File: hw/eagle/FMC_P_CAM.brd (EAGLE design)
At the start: 100 x 80 mm, 1 part, among them J1 FMC-LPC

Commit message: update board
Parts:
- added U1: SN74AVCH16T245_DGV_48, SN74AVCH16T245_DGV_48:DGV48
- moved J1 6.48 mm to (17.8, 34.3)
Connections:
- removed net VADJ: J1.H40
- new net +12V: J1.C35, J1.C37
- new net +3V3: J1.C39, J1.D36, J1.D38, J1.D40
- new net FMC_CAM1_D0: J1.D15
- new net FMC_CAM1_D1: J1.D14
- new net FMC_CAM1_D2: J1.C15
- new net FMC_CAM1_D3: J1.C14
- new net FMC_CAM1_D8: J1.D12
- new net FMC_CAM1_D9: J1.D11
- new net FMC_CAM1_HREF: J1.C11
- new net FMC_CAM1_PWDN: J1.C23
- new net FMC_CAM1_RST: J1.D8
- new net FMC_CAM1_VSYNC: J1.C10
- new net FMC_CAM2_HREF: J1.D21
- new net FMC_CAM2_PWDN: J1.C18
- new net FMC_CAM2_RSVD4: J1.D18
- new net FMC_CAM2_RSVD5: J1.D17
- new net FMC_CAM2_RSVD6: J1.C19
- new net FMC_CAM2_VSYNC: J1.D20
- new net FMC_DVO_D10: J1.D24
- new net FMC_DVO_D11: J1.D23
- new net FMC_DVO_D6: J1.D27
- new net FMC_DVO_D7: J1.D26
- new net FMC_DVO_D8: J1.C27
- new net FMC_DVO_D9: J1.C26
- new net FMC_DVO_IDCK+: J1.C22
- new net FMC_GA0: J1.C34
- new net FMC_GA1: J1.D35
- new net FMC_GPIO3: J1.D9
- new net FMC_SCL: J1.C30
- new net FMC_SDA: J1.C31
- new net N$4: J1.D30, J1.D31
- new net PG_C2M: J1.D1
- net FMC_CAM1_RSVD0: now also U1.22
- net FMC_CAM1_RSVD1: now also U1.20
- net FMC_CAM1_RSVD2: now also U1.19
- net FMC_CAM1_RSVD3: now also U1.17
- net FMC_CAM1_RSVD4: now also U1.16
- net FMC_CAM1_RSVD6: now also U1.13
- net GND: now also J1.C1, J1.C12, J1.C13, J1.C16, J1.C17, J1.C20, J1.C21, J1.C24, J1.C25, J1.C28, J1.C29, J1.C32, J1.C33, J1.C36, J1.C38, J1.C4, J1.C40, J1.C5, J1.C8, J1.C9, J1.D10, J1.D13, J1.D16, J1.D19, J1.D2, J1.D22, J1.D25, J1.D28, J1.D3, J1.D37, J1.D39, J1.D6, J1.D7, U1.10, U1.15, U1.21, U1.28, U1.34, U1.39, U1.4, U1.45
- net VDD: now also J1.H40, U1.18, U1.31, U1.42, U1.7

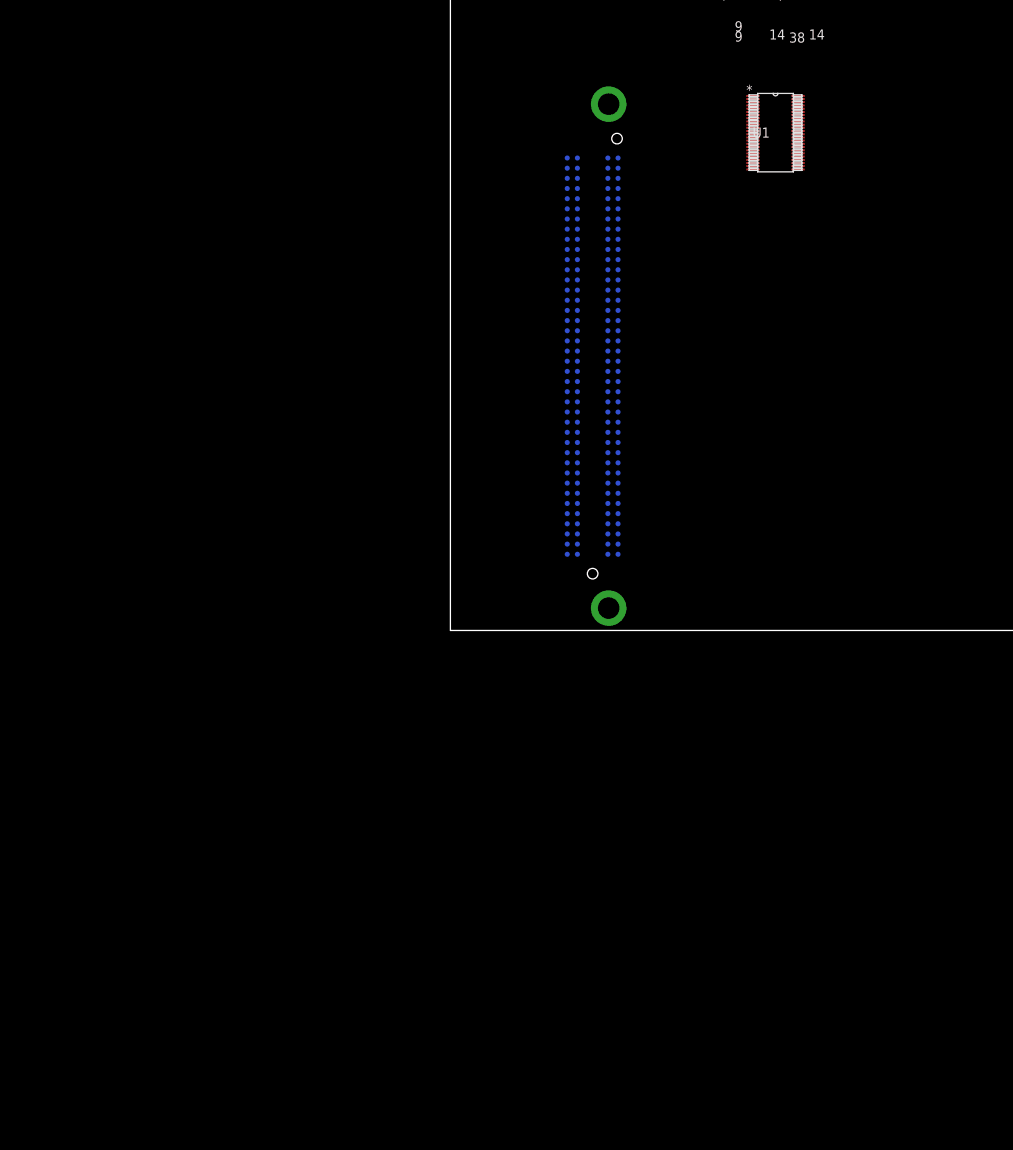
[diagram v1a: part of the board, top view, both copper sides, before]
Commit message: update schematic
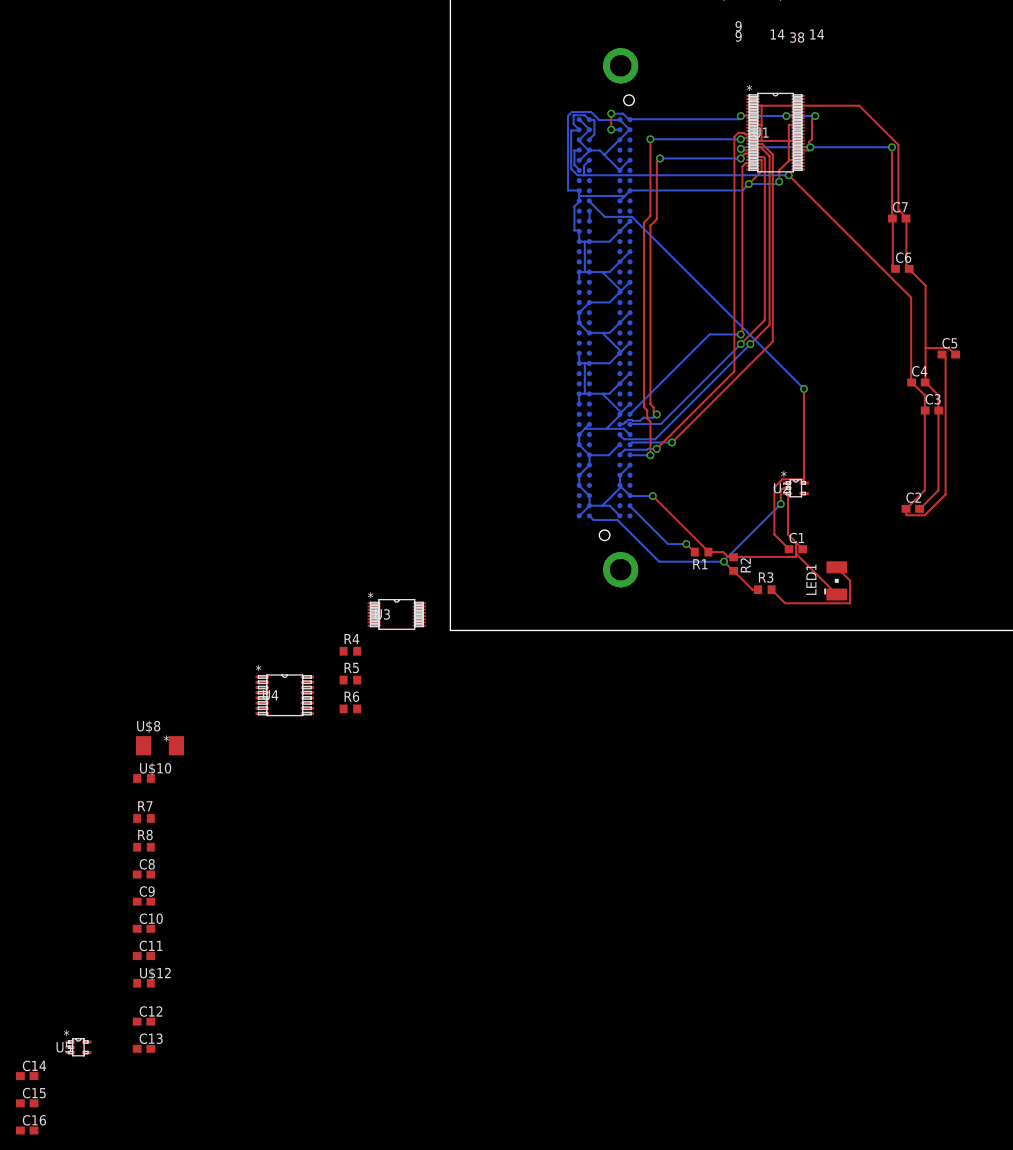
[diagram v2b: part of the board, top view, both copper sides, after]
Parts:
- added C1, C2, C3, C4, C5, C6, C7: (no value), resistor:C0603
- added C10, C11, C12, C13, C14, C15, C16, C8, C9: (no value), my-rcl:C0603
- added LED1: LY_T679-D2E2-1, led:PLCC2
- added R1, R2, R3: 4K7, resistor:R0603
- added R4, R5, R6, R7, R8: (no value), resistor:R0603
- added U$10, U$12: L-MY, my-rcl:R0603
- added U$8: (no value), CX5032GB (CX-53F):CX5032GB
- added U2: SN74LVC1G14_DCK_5, SN74LVC1G14_DCK_5:DCK5
- added U3: PCA9546A_DGV_16, PCA9546A_DGV_16:DGV16
- added U4: CDCE925_PW_16, CDCE925_PW_16:PW16
- added U5: TPS71718_DCK_5, TPS71718_DCK_5:DCK5
- moved J1 5.03 mm to (19.3, 39.1)
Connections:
- net +12V renamed 12P0V
- removed net +3V3: J1.C39, J1.D36, J1.D38, J1.D40
- removed net VDD: J1.G39, J1.H40, U1.18, U1.31, U1.42, U1.7
- new net 3P3AUX: C1.1, J1.D32, U2.5
- new net 3P3V: C14.1, C2.1, C3.1, C4.1, C5.1, J1.C39, J1.D36, J1.D38, J1.D40, U1.24, U1.31, U1.42, U5.1, U5.3
- new net CAM1_SCL: U3.7
- new net CAM1_SDA: U3.6
- new net CAM2_SCL: U3.5
- new net CAM2_SDA: U3.4
- new net EN#: U1.25, U1.48, U2.4
- new net HDMI_SCL: U3.12
- new net HDMI_SDA: U3.11
- new net N$10: C12.1, U4.7
- new net N$11: C13.1, U4.8
- new net N$13: C15.1, U5.4
- new net N$2: LED1.A, R3.2
- new net N$3: U$8.2, U4.1
- new net N$5: U$8.1, U4.16
- new net N$6: C8.1, R7.2, R8.2, U$10.2, U4.3
- new net N$7: R8.1, U4.2
- new net N$8: R7.1, U4.4
- new net N$9: C10.1, C11.1, U$12.2, U4.6, U4.9
- new net REG_1P8V: C16.1, U$10.1, U5.5
- new net TMDS_PLL_SCL: U3.10, U4.14
- new net TMDS_PLL_SDA: U3.9, U4.15
- new net VADJ: C6.1, C7.1, C9.1, J1.G39, J1.H40, R4.2, R5.2, R6.2, U$12.1, U1.18, U1.7, U3.16
- net FMC_CAM1_PCLK: now also U1.23
- net FMC_CAM1_PWDN: now also U1.3
- net FMC_CAM1_RST: now also U1.2
- net FMC_CAM1_RSVD5: now also U1.14
- net FMC_CAM2_PWDN: now also U1.12
- net FMC_CAM2_RST: now also U1.11
- net FMC_FRSTN_M2C_L: now also R1.2
- net GND: now also C1.2, C10.2, C11.2, C14.2, C15.2, C16.2, C2.2, C3.2, C4.2, C5.2, C6.2, C7.2, C8.2, LED1.C, R1.1, R2.1, U1.1, U2.3, U3.1, U3.13, U3.2, U3.8, U4.12, U4.5, U5.2
- net I2C_SW_RST: now also R4.1, U3.3
- net MUX_SCL: now also R6.1, U3.14
- net MUX_SDA: now also R5.1, U3.15
- net PG_C2M: now also R2.2, R3.1, U2.2
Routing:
- net GND: track 0.00 -> 322.1 mm, vias 0 -> 3
- net 3P3V: track 0.00 -> 117.5 mm, vias 0 -> 1
- net VADJ: track 0.00 -> 74.5 mm, vias 0 -> 8
- net 3P3AUX: track 0.00 -> 61.0 mm, vias 0 -> 1
- net FMC_CAM1_RSVD5: track 0.00 -> 55.7 mm, vias 0 -> 3
- net FMC_CAM1_RSVD6: track 0.00 -> 50.6 mm, vias 0 -> 1
- net FMC_CAM1_RSVD2: track 0.00 -> 50.0 mm, vias 0 -> 3
- net FMC_CAM1_RSVD4: track 0.00 -> 49.6 mm, vias 0 -> 1
- net FMC_CAM1_RSVD3: track 0.00 -> 48.6 mm, vias 0 -> 1
- net FMC_CAM1_RSVD1: track 0.00 -> 44.0 mm, vias 0 -> 1
- net FMC_CAM1_RSVD0: track 0.00 -> 40.6 mm, vias 0 -> 1
- net PG_C2M: track 0.00 -> 37.8 mm, vias 0 -> 2
- net N$2: track 0.00 -> 15.7 mm
- net FMC_FRSTN_M2C_L: track 0.00 -> 10.5 mm, vias 0 -> 1
- net 12P0V: track 0.00 -> 3.39 mm
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
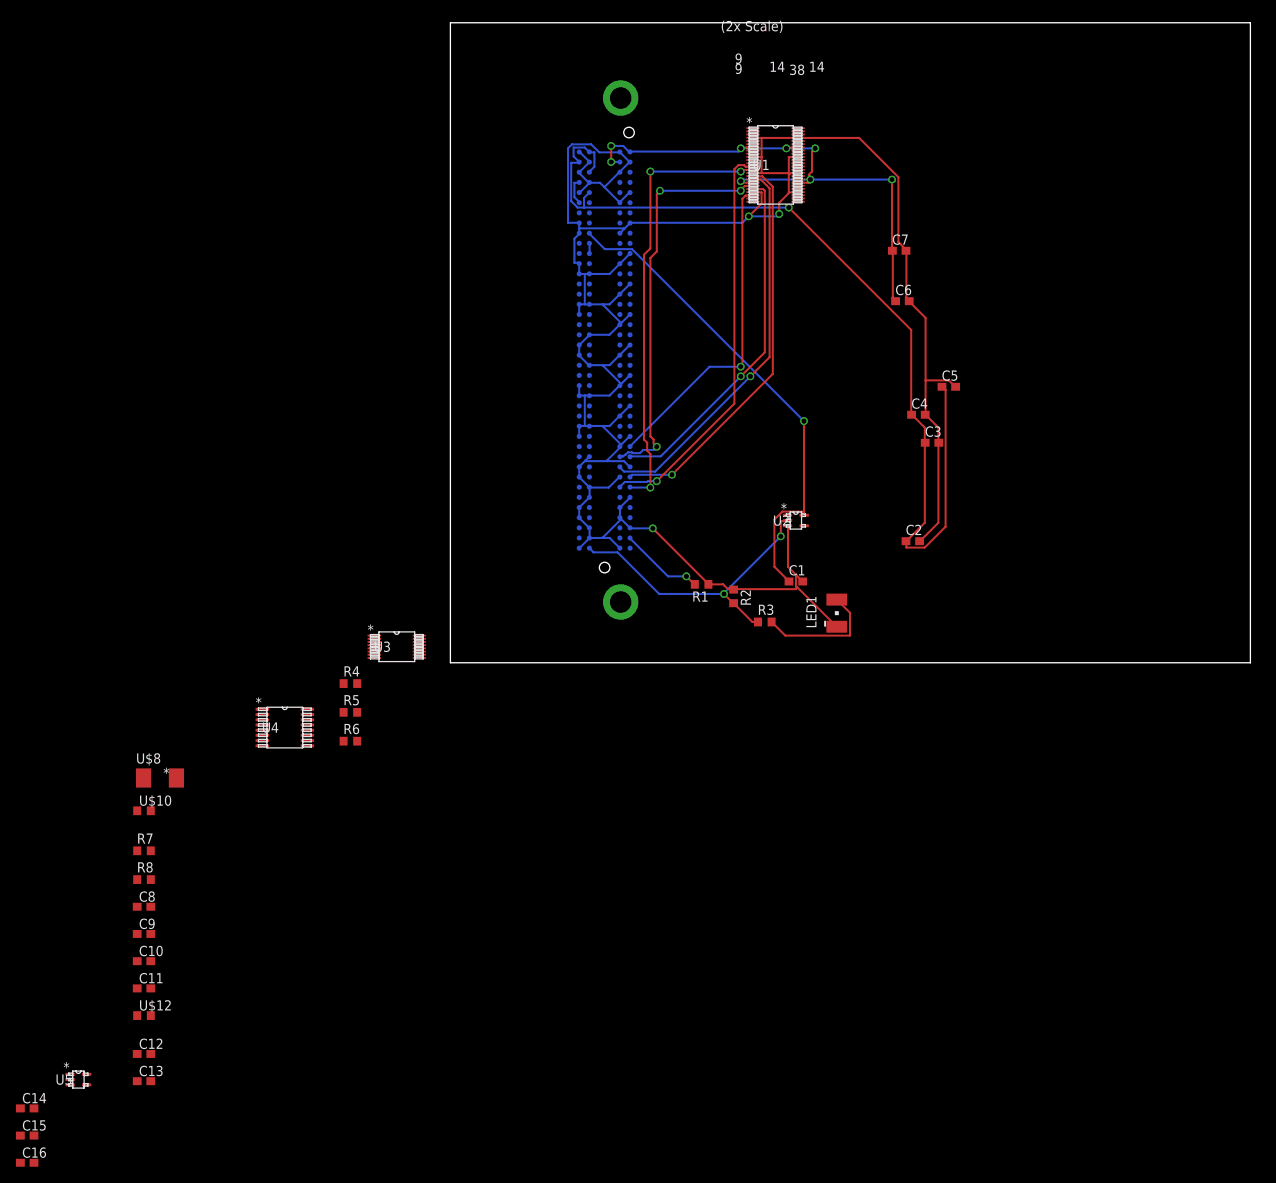
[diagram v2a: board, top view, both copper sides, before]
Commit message: add user defined library
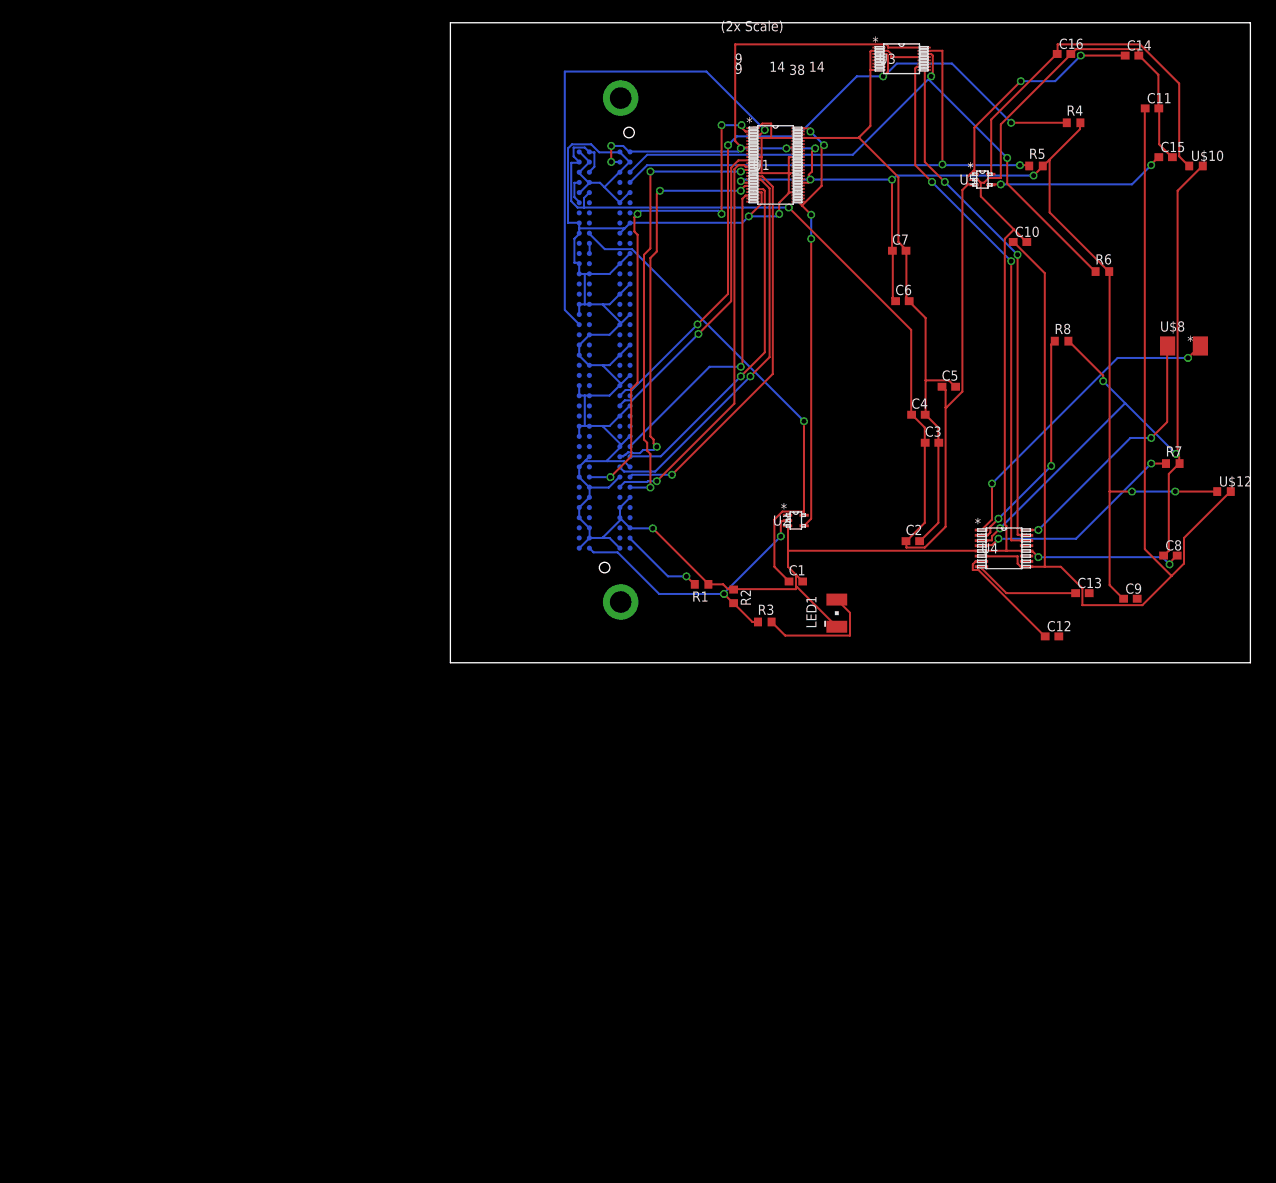
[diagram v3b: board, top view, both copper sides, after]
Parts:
- moved C14 190.8 mm to (85.2, 75.9)
- moved C16 189.8 mm to (76.7, 76.1)
- moved C15 187.6 mm to (89.4, 63.2)
- moved C11 167.3 mm to (87.7, 69.3)
- moved U5 159.5 mm to (66.5, 60.4)
- moved U$10 154.2 mm to (93.2, 62.1)
- moved U$12 150.1 mm to (96.7, 21.4)
- moved C10 141.7 mm to (71.2, 52.6)
- moved U$8 138.9 mm to (91.7, 39.6)
- moved R7 137.4 mm to (90.3, 24.9)
- moved C8 135.6 mm to (90.0, 13.4)
- moved R8 133.0 mm to (76.4, 40.2)
- moved C13 132.2 mm to (79.0, 8.70)
- moved C9 130.2 mm to (85.0, 8.00)
- moved C12 124.9 mm to (75.2, 3.30)
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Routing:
- net GND: track 322.1 -> 494.0 mm, vias 3 -> 5
- net N$9: track 0.00 -> 145.4 mm
- net VADJ: track 74.5 -> 210.9 mm, vias 8 -> 11
- net N$6: track 0.00 -> 96.5 mm, vias 0 -> 3
- net I2C_SW_RST: track 0.00 -> 91.1 mm, vias 0 -> 4
- net MUX_SCL: track 0.00 -> 79.6 mm, vias 0 -> 2
- net MUX_SDA: track 0.00 -> 67.5 mm, vias 0 -> 2
- net TMDS_PLL_SCL: track 0.00 -> 67.1 mm, vias 0 -> 2
- net TMDS_PLL_SDA: track 0.00 -> 64.2 mm, vias 0 -> 2
- net FMC_CAM1_RST: track 0.00 -> 63.6 mm, vias 0 -> 5
- net FMC_CAM1_PWDN: track 0.00 -> 62.1 mm, vias 0 -> 1
- net 3P3V: track 117.5 -> 178.1 mm, vias 1 -> 3
- net EN#: track 0.00 -> 54.6 mm, vias 0 -> 4
- net REG_1P8V: track 0.00 -> 47.8 mm
- net N$3: track 0.00 -> 39.5 mm, vias 0 -> 2
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
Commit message: update board schematic
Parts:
- removed C1: (no value), resistor:C0603
- removed R2: 4K7, resistor:R0603
- removed U$8: (no value), CX5032GB (CX-53F):CX5032GB
- added C101: 100nF, resistor:C0603
- added C305, C306, C307, C308, C309, C310, C311, C312, C313, C314, C315, C316, C503: 100nF, rcl:C0603
- added C500: 15nF, rcl:C0603
- added C501: 330pF, rcl:C0603
- added C502: 12pF, rcl:C0603
- added C507: 10uF 16V, rcl:C0603
- added C508: 47uF 10V, rcl:C0603
- added C509, C510: 2n2F, rcl:C0603
- added D1: MBRS130LT3, diode:SMB
- added PAD1, PAD10, PAD11, PAD2, PAD3, PAD4, PAD5, PAD6, PAD7, PAD8, PAD9: (no value), wirepad:1,6/0,8
- added Q1: 27MHz, special:Q
- added R106: 4K7 DNI, resistor:R0603
- added R202, R203, R205, R206, R207, R208, R209, R210: 4K7, resistor:R0603
- added R500: 348K, rcl:R0603
- added R501: 78K7, rcl:R0603
- added R502: 40K2, rcl:R0603
- added R503: 10K, rcl:R0603
- added R504: 1K87, rcl:R0603
- added R506: 36K5, rcl:R0603
- added U$23, U$24: L-MY, my-rcl:R0603
- added U6, U7: SN74AVCH16T245_DGV_48, SN74AVCH16T245_DGV_48:DGV48
- added U8: TPS54140_DGQ_10, TPS54140_DGQ_10:DGQ10_1P88X1P57
- C102, C103, C104, C105, C106, C107, C200, C201, C202, C203, C209, C210: value (none) -> 100nF
- C206, C208: value (none) -> 1uF
- C207: value (none) -> 10nF
- R105: value 4K7 -> 33R DNI
- R200, R201, R204, R212: value (none) -> 4K7
- R211: value (none) -> 4K7 DNI
- moved U2 47.3 mm to (34.1, 64.2), turned to 180 degrees
- moved U1 44.4 mm to (48.8, 18.6), flipped to the bottom, turned to 180.5 degrees
- moved U3 32.8 mm to (68.3, 44.9)
- moved U4 14.7 mm to (75.5, 27.6), turned to 90 degrees
- renumbered C10 to C202, C11 to C201, C12 to C209, C13 to C210, C14 to C206, C15 to C207, C16 to C208, C2 to C102, C3 to C103, C4 to C104, C5 to C105, C6 to C106, C7 to C107, C8 to C203, C9 to C200, R1 to R104, R3 to R105, R4 to R204, R5 to R201, R6 to R200, R7 to R211, R8 to R212
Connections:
- new net CAM1_XCLK: C210.2
- new net CAM2_XCLK: C209.2
- new net N$15: C507.1, C510.1, R500.2, U$23.2, U8.2
- new net N$16: C503.1, U8.1
- new net N$17: C503.2, D1.C, U$24.1, U8.10
- new net N$19: R500.1, R501.2, U8.3
- new net N$20: C500.1, U8.4
- new net N$21: R502.2, U8.5
- new net N$22: J1.H1, PAD1.1
- new net N$23: C502.1, R506.2, U8.8
- new net N$24: C501.1, R506.1
- new net N$25: R503.1, R504.2, U8.7
- new net N$26: J1.D4, PAD3.1
- new net N$27: J1.D5, PAD4.1
- new net N$28: J1.D29, PAD5.1
- new net N$29: J1.D33, PAD6.1
- new net N$30: J1.D34, PAD7.1
- new net N$31: J1.C2, PAD8.1
- new net N$32: J1.C3, PAD9.1
- new net N$33: J1.C6, PAD10.1
- new net N$34: J1.C7, PAD11.1
- new net PGOOD: U8.6
- new net REG_5P0V: C508.1, R209.2, R210.2, R503.2, U$24.2
- net 12P0V: now also C509.1, U$23.1
- net 3P3AUX: now also C101.1; no longer C1.1
- net 3P3V: now also C305.1, C306.1, C309.1, C310.1, C313.1, C314.1, R202.2, R203.2, R205.2, R206.2, R207.2, R208.2, U6.1, U6.24, U6.31, U6.42, U7.1, U7.24, U7.31, U7.42
- net CAM1_SCL: now also R203.1
- net CAM1_SDA: now also R202.1
- net CAM2_SCL: now also R206.1
- net CAM2_SDA: now also R205.1
- net EN#: now also U6.25, U6.48, U7.25, U7.48
- net FMC_CAM1_D0: now also U6.17
- net FMC_CAM1_D1: now also U6.16
- net FMC_CAM1_D2: now also U6.14
- net FMC_CAM1_D3: now also U6.13
- net FMC_CAM1_D4: now also U6.12
- net FMC_CAM1_D5: now also U6.11
- net FMC_CAM1_D6: now also U6.9
- net FMC_CAM1_D7: now also U6.8
- net FMC_CAM1_D8: now also U6.6
- net FMC_CAM1_D9: now also U6.5
- net FMC_CAM1_HREF: now also U6.3
- net FMC_CAM1_VSYNC: now also U6.2
- net FMC_CAM2_D0: now also U7.23
- net FMC_CAM2_D1: now also U7.22
- net FMC_CAM2_D2: now also U7.20
- net FMC_CAM2_D3: now also U7.19
- net FMC_CAM2_D4: now also U7.17
- net FMC_CAM2_D5: now also U7.16
- net FMC_CAM2_D6: now also U7.14
- net FMC_CAM2_D7: now also U7.13
- net FMC_CAM2_D8: now also U7.12
- net FMC_CAM2_D9: now also U7.11
- net FMC_CAM2_HREF: now also U7.9
- net FMC_CAM2_PCLK: now also U7.6
- net FMC_CAM2_RSVD0: now also U7.5
- net FMC_CAM2_RSVD1: now also U7.3
- net FMC_CAM2_RSVD2: now also U7.2
- net FMC_CAM2_RSVD3: now also U6.23
- net FMC_CAM2_RSVD4: now also U6.22
- net FMC_CAM2_RSVD5: now also U6.20
- net FMC_CAM2_RSVD6: now also U6.19
- net FMC_CAM2_VSYNC: now also U7.8
- net GND: now also C101.2, C200.2, C305.2, C306.2, C307.2, C308.2, C309.2, C310.2, C311.2, C312.2, C313.2, C314.2, C315.2, C316.2, C500.2, C501.2, C502.2, C507.2, C508.2, C509.2, C510.2, D1.A, R106.1, R501.1, R502.1, R504.1, U6.10, U6.15, U6.21, U6.28, U6.34, U6.39, U6.4, U6.45, U7.10, U7.15, U7.21, U7.28, U7.34, U7.39, U7.4, U7.45, U8.9; no longer C1.2, R2.1
- net HDMI_SCL: now also R210.1
- net HDMI_SDA: now also R209.1
- net N$1: now also PAD2.1
- net N$3: now also Q1.1; no longer U$8.2
- net N$5: now also Q1.2; no longer U$8.1
- net PG_C2M: now also R106.2; no longer R2.2
- net TMDS_PLL_SCL: now also R208.1
- net TMDS_PLL_SDA: now also R207.1
- net VADJ: now also C307.1, C308.1, C311.1, C312.1, C315.1, C316.1, U6.18, U6.7, U7.18, U7.7
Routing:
- net GND: track 494.0 -> 0.00 mm, vias 5 -> 0
- net VADJ: track 210.9 -> 0.00 mm, vias 11 -> 0
- net 3P3V: track 178.1 -> 0.00 mm, vias 3 -> 0
- net N$9: track 145.4 -> 0.00 mm
- net N$6: track 96.5 -> 0.00 mm, vias 3 -> 0
- net I2C_SW_RST: track 91.1 -> 0.00 mm, vias 4 -> 0
- net MUX_SCL: track 79.6 -> 0.00 mm, vias 2 -> 0
- net MUX_SDA: track 67.5 -> 0.00 mm, vias 2 -> 0
- net TMDS_PLL_SCL: track 67.1 -> 0.00 mm, vias 2 -> 0
- net TMDS_PLL_SDA: track 64.2 -> 0.00 mm, vias 2 -> 0
- net FMC_CAM1_RST: track 63.6 -> 0.00 mm, vias 5 -> 0
- net FMC_CAM1_PWDN: track 62.1 -> 0.00 mm, vias 1 -> 0
- net 3P3AUX: track 61.0 -> 0.00 mm, vias 1 -> 0
- net FMC_CAM1_RSVD5: track 55.7 -> 0.00 mm, vias 3 -> 0
- net EN#: track 54.6 -> 0.00 mm, vias 4 -> 0
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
